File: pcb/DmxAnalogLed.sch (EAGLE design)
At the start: 55 parts, among them IC2 7805TV, J1 RS485, J2 POWER_JACKPTH, J3 RS485, Q1 16MHz 10ppm, U1 ARDUINO_LEONARDO-REV3B_SMARTP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, U2 SN75176ASOIC, X1 USBPTH

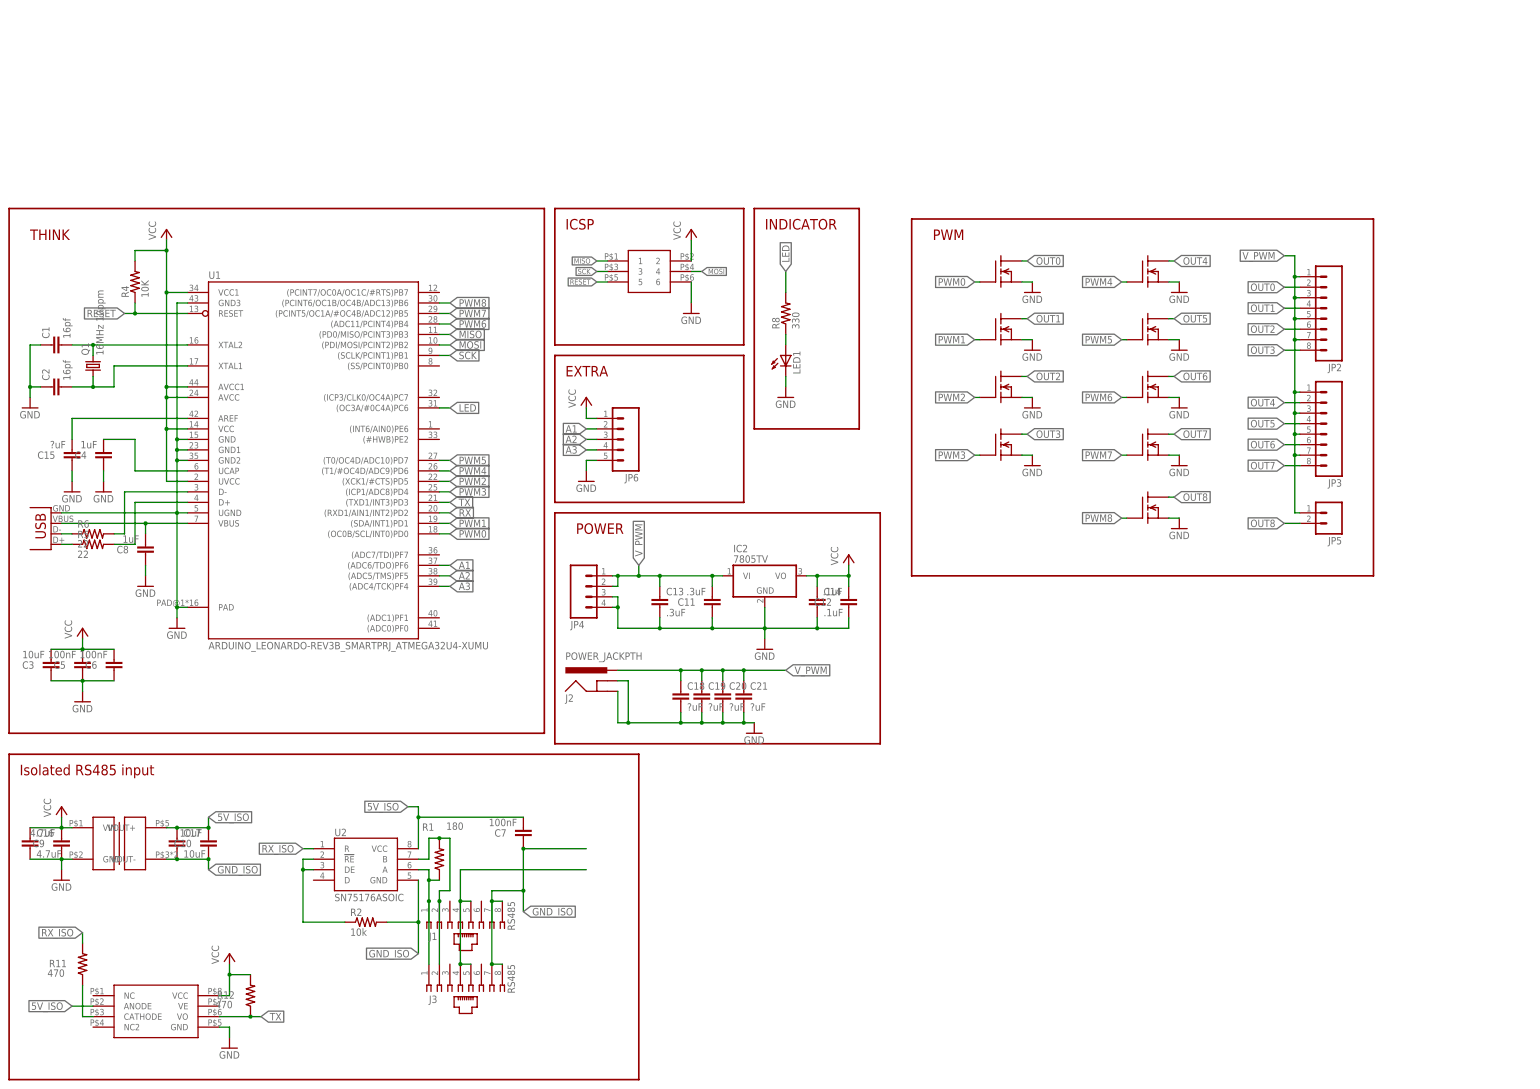
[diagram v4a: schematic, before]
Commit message: Re-wire PWMs for hardware PWM generation. Bugfix: Serial should be connected to AVR RX, not TX
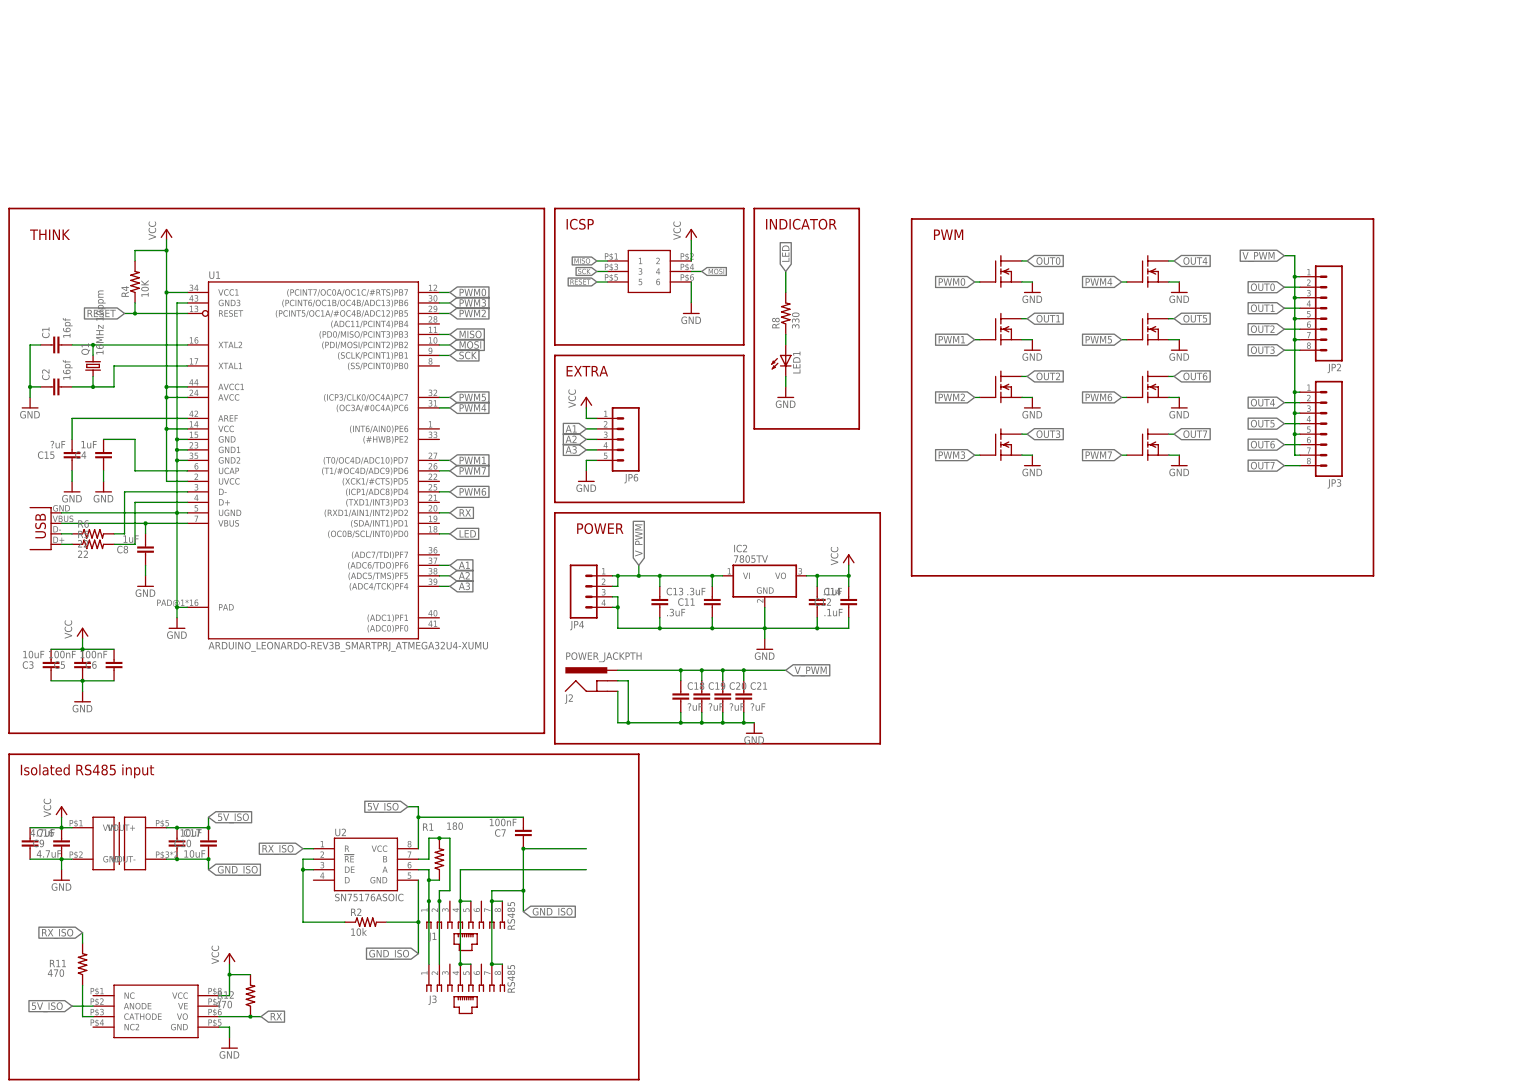
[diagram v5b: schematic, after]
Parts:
- removed JP5: (no value), SparkFun:M023.5MM
- removed U$11: N_MOSFET, blinkiverse:N_MOSFET
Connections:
- removed net OUT8: JP5.2, U$11.D
- removed net PWM8: U$11.G, U1.(PCINT6/OC1B/OC4B/ADC13)PB6
- removed net TX: R12.1, U$12.VO, U1.(TXD1/INT3)PD3
- net GND: no longer U$11.S
- net LED: now also U1.(OC0B/SCL/INT0)PD0; no longer U1.(OC3A/#0C4A)PC6
- net PWM0: now also U1.(PCINT7/OC0A/OC1C/#RTS)PB7; no longer U1.(OC0B/SCL/INT0)PD0
- net PWM1: now also U1.(T0/OC4D/ADC10)PD7; no longer U1.(SDA/INT1)PD1
- net PWM2: now also U1.(PCINT5/OC1A/#OC4B/ADC12)PB5; no longer U1.(XCK1/#CTS)PD5
- net PWM3: now also U1.(PCINT6/OC1B/OC4B/ADC13)PB6; no longer U1.(ICP1/ADC8)PD4
- net PWM4: now also U1.(OC3A/#0C4A)PC6; no longer U1.(T1/#OC4D/ADC9)PD6
- net PWM5: now also U1.(ICP3/CLK0/OC4A)PC7; no longer U1.(T0/OC4D/ADC10)PD7
- net PWM6: now also U1.(ICP1/ADC8)PD4; no longer U1.(ADC11/PCINT4)PB4
- net PWM7: now also U1.(T1/#OC4D/ADC9)PD6; no longer U1.(PCINT5/OC1A/#OC4B/ADC12)PB5
- net RX: now also R12.1, U$12.VO
- net V_PWM: no longer JP5.1
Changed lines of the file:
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@@
 <part name="GND2" library="SparkFun" deviceset="GND" device=""/>
 <part name="P+9" library="supply1" deviceset="VCC" device=""/>
-<part name="U$11" library="blinkiverse" deviceset="N_MOSFET" device=""/>
-<part name="GND8" library="supply1" deviceset="GND" device=""/>
-<part name="JP5" library="SparkFun" deviceset="M02" device="3.5MM"/>
 <part name="C8" library="SparkFun" deviceset="CAP" device="0805" value="1uF"/>
 <part name="GND18" library="supply1" deviceset="GND" device=""/>
@@
 <instance part="GND2" gate="1" x="22.86" y="-124.46"/>
 <instance part="P+9" gate="VCC" x="22.86" y="-101.6"/>
-<instance part="U$11" gate="G$1" x="243.84" y="6.35"/>
-<instance part="GND8" gate="1" x="252.73" y="1.27"/>
-<instance part="JP5" gate="G$1" x="289.56" y="5.08" rot="R180"/>
 <instance part="C8" gate="G$1" x="2.54" y="-2.54" smashed="yes" rot="R180">
 <attribute name="NAME" x="-1.524" y="-2.921" size="1.778" layer="95" rot="R180"/>
@@
 <wire x1="20.32" y1="-119.38" x2="22.86" y2="-119.38" width="0.1524" layer="91"/>
 <wire x1="22.86" y1="-119.38" x2="22.86" y2="-121.92" width="0.1524" layer="91"/>
-</segment>
-<segment>
-<pinref part="U$11" gate="G$1" pin="S"/>
-<wire x1="250.19" y1="3.81" x2="252.73" y2="3.81" width="0.1524" layer="91"/>
-<pinref part="GND8" gate="1" pin="GND"/>
 </segment>
 <segment>
@@
 <label x="76.2" y="5.08" size="1.778" layer="95" xref="yes"/>
 </segment>
-</net>
-<net name="TX" class="0">
-<segment>
-<pinref part="U1" gate="G$1" pin="(TXD1/INT3)PD3"/>
-<wire x1="73.66" y1="7.62" x2="76.2" y2="7.62" width="0.1524" layer="91"/>
-<label x="76.2" y="7.62" size="1.778" layer="95" xref="yes"/>
-</segment>
 <segment>
 <pinref part="U$12" gate="G$1" pin="VO"/>
@@
 </segment>
 <segment>
-<pinref part="U1" gate="G$1" pin="(OC0B/SCL/INT0)PD0"/>
-<wire x1="73.66" y1="0" x2="76.2" y2="0" width="0.1524" layer="91"/>
-<label x="76.2" y="0" size="1.778" layer="95" xref="yes"/>
+<pinref part="U1" gate="G$1" pin="(PCINT7/OC0A/OC1C/#RTS)PB7"/>
+<wire x1="73.66" y1="58.42" x2="76.2" y2="58.42" width="0.1524" layer="91"/>
+<label x="76.2" y="58.42" size="1.778" layer="95" xref="yes"/>
 </segment>
 </net>
@@
 </segment>
 <segment>
-<pinref part="U1" gate="G$1" pin="(SDA/INT1)PD1"/>
-<wire x1="73.66" y1="2.54" x2="76.2" y2="2.54" width="0.1524" layer="91"/>
-<label x="76.2" y="2.54" size="1.778" layer="95" xref="yes"/>
+<pinref part="U1" gate="G$1" pin="(T0/OC4D/ADC10)PD7"/>
+<wire x1="73.66" y1="17.78" x2="76.2" y2="17.78" width="0.1524" layer="91"/>
+<label x="76.2" y="17.78" size="1.778" layer="95" xref="yes"/>
 </segment>
 </net>
@@
 </segment>
 <segment>
-<pinref part="U1" gate="G$1" pin="(XCK1/#CTS)PD5"/>
-<wire x1="73.66" y1="12.7" x2="76.2" y2="12.7" width="0.1524" layer="91"/>
-<label x="76.2" y="12.7" size="1.778" layer="95" xref="yes"/>
+<pinref part="U1" gate="G$1" pin="(PCINT5/OC1A/#OC4B/ADC12)PB5"/>
+<wire x1="73.66" y1="53.34" x2="76.2" y2="53.34" width="0.1524" layer="91"/>
+<label x="76.2" y="53.34" size="1.778" layer="95" xref="yes"/>
 </segment>
 </net>
@@
 </segment>
 <segment>
+<pinref part="U1" gate="G$1" pin="(PCINT6/OC1B/OC4B/ADC13)PB6"/>
+<wire x1="73.66" y1="55.88" x2="76.2" y2="55.88" width="0.1524" layer="91"/>
+<label x="76.2" y="55.88" size="1.778" layer="95" xref="yes"/>
+</segment>
+</net>
+<net name="PWM4" class="0">
+<segment>
+<pinref part="U$6" gate="G$1" pin="G"/>
+<wire x1="240.03" y1="60.96" x2="238.76" y2="60.96" width="0.1524" layer="91"/>
+<label x="238.76" y="60.96" size="1.778" layer="95" rot="R180" xref="yes"/>
+</segment>
+<segment>
+<pinref part="U1" gate="G$1" pin="(OC3A/#0C4A)PC6"/>
+<wire x1="73.66" y1="30.48" x2="76.2" y2="30.48" width="0.1524" layer="91"/>
+<label x="76.2" y="30.48" size="1.778" layer="95" xref="yes"/>
+</segment>
+</net>
+<net name="PWM5" class="0">
+<segment>
+<pinref part="U$7" gate="G$1" pin="G"/>
+<wire x1="240.03" y1="46.99" x2="238.76" y2="46.99" width="0.1524" layer="91"/>
+<label x="238.76" y="46.99" size="1.778" layer="95" rot="R180" xref="yes"/>
+</segment>
+<segment>
+<pinref part="U1" gate="G$1" pin="(ICP3/CLK0/OC4A)PC7"/>
+<wire x1="73.66" y1="33.02" x2="76.2" y2="33.02" width="0.1524" layer="91"/>
+<label x="76.2" y="33.02" size="1.778" layer="95" xref="yes"/>
+</segment>
+</net>
+<net name="PWM6" class="0">
+<segment>
+<pinref part="U$8" gate="G$1" pin="G"/>
+<wire x1="240.03" y1="33.02" x2="238.76" y2="33.02" width="0.1524" layer="91"/>
+<label x="238.76" y="33.02" size="1.778" layer="95" rot="R180" xref="yes"/>
+</segment>
+<segment>
 <pinref part="U1" gate="G$1" pin="(ICP1/ADC8)PD4"/>
 <wire x1="73.66" y1="10.16" x2="76.2" y2="10.16" width="0.1524" layer="91"/>
@@
 </segment>
 </net>
-<net name="PWM4" class="0">
-<segment>
-<pinref part="U$6" gate="G$1" pin="G"/>
-<wire x1="240.03" y1="60.96" x2="238.76" y2="60.96" width="0.1524" layer="91"/>
-<label x="238.76" y="60.96" size="1.778" layer="95" rot="R180" xref="yes"/>
+<net name="PWM7" class="0">
+<segment>
+<pinref part="U$9" gate="G$1" pin="G"/>
+<wire x1="240.03" y1="19.05" x2="238.76" y2="19.05" width="0.1524" layer="91"/>
+<label x="238.76" y="19.05" size="1.778" layer="95" rot="R180" xref="yes"/>
 </segment>
 <segment>
@@
 <wire x1="73.66" y1="15.24" x2="76.2" y2="15.24" width="0.1524" layer="91"/>
 <label x="76.2" y="15.24" size="1.778" layer="95" xref="yes"/>
-</segment>
-</net>
-<net name="PWM5" class="0">
-<segment>
-<pinref part="U$7" gate="G$1" pin="G"/>
-<wire x1="240.03" y1="46.99" x2="238.76" y2="46.99" width="0.1524" layer="91"/>
-<label x="238.76" y="46.99" size="1.778" layer="95" rot="R180" xref="yes"/>
-</segment>
-<segment>
-<pinref part="U1" gate="G$1" pin="(T0/OC4D/ADC10)PD7"/>
-<wire x1="73.66" y1="17.78" x2="76.2" y2="17.78" width="0.1524" layer="91"/>
-<label x="76.2" y="17.78" size="1.778" layer="95" xref="yes"/>
-</segment>
-</net>
-<net name="PWM6" class="0">
-<segment>
-<pinref part="U$8" gate="G$1" pin="G"/>
-<wire x1="240.03" y1="33.02" x2="238.76" y2="33.02" width="0.1524" layer="91"/>
-<label x="238.76" y="33.02" size="1.778" layer="95" rot="R180" xref="yes"/>
-</segment>
-<segment>
-<pinref part="U1" gate="G$1" pin="(ADC11/PCINT4)PB4"/>
-<wire x1="73.66" y1="50.8" x2="76.2" y2="50.8" width="0.1524" layer="91"/>
-<label x="76.2" y="50.8" size="1.778" layer="95" xref="yes"/>
-</segment>
-</net>
-<net name="PWM7" class="0">
-<segment>
-<pinref part="U$9" gate="G$1" pin="G"/>
-<wire x1="240.03" y1="19.05" x2="238.76" y2="19.05" width="0.1524" layer="91"/>
-<label x="238.76" y="19.05" size="1.778" layer="95" rot="R180" xref="yes"/>
-</segment>
-<segment>
-<pinref part="U1" gate="G$1" pin="(PCINT5/OC1A/#OC4B/ADC12)PB5"/>
-<wire x1="73.66" y1="53.34" x2="76.2" y2="53.34" width="0.1524" layer="91"/>
-<label x="76.2" y="53.34" size="1.778" layer="95" xref="yes"/>
 </segment>
 </net>
@@
 <junction x="280.67" y="29.21"/>
 <junction x="280.67" y="24.13"/>
-<wire x1="280.67" y1="19.05" x2="280.67" y2="5.08" width="0.1524" layer="91"/>
-<pinref part="JP5" gate="G$1" pin="1"/>
-<wire x1="280.67" y1="5.08" x2="281.94" y2="5.08" width="0.1524" layer="91"/>
-<junction x="280.67" y="19.05"/>
 </segment>
 <segment>
@@
 </segment>
 </net>
-<net name="PWM8" class="0">
-<segment>
-<pinref part="U$11" gate="G$1" pin="G"/>
-<wire x1="240.03" y1="3.81" x2="238.76" y2="3.81" width="0.1524" layer="91"/>
-<label x="238.76" y="3.81" size="1.778" layer="95" rot="R180" xref="yes"/>
-</segment>
-<segment>
-<pinref part="U1" gate="G$1" pin="(PCINT6/OC1B/OC4B/ADC13)PB6"/>
-<wire x1="73.66" y1="55.88" x2="76.2" y2="55.88" width="0.1524" layer="91"/>
-<label x="76.2" y="55.88" size="1.778" layer="95" xref="yes"/>
-</segment>
-</net>
-<net name="OUT8" class="0">
-<segment>
-<pinref part="U$11" gate="G$1" pin="D"/>
-<wire x1="250.19" y1="8.89" x2="251.46" y2="8.89" width="0.1524" layer="91"/>
-<label x="251.46" y="8.89" size="1.778" layer="95" xref="yes"/>
-</segment>
-<segment>
-<pinref part="JP5" gate="G$1" pin="2"/>
-<wire x1="281.94" y1="2.54" x2="278.13" y2="2.54" width="0.1524" layer="91"/>
-<label x="278.13" y="2.54" size="1.778" layer="95" rot="R180" xref="yes"/>
-</segment>
-</net>
 <net name="N$10" class="0">
 <segment>
@@
 <net name="LED" class="0">
 <segment>
-<pinref part="U1" gate="G$1" pin="(OC3A/#0C4A)PC6"/>
-<wire x1="73.66" y1="30.48" x2="76.2" y2="30.48" width="0.1524" layer="91"/>
-<label x="76.2" y="30.48" size="1.778" layer="95" xref="yes"/>
-</segment>
-<segment>
 <wire x1="157.48" y1="58.42" x2="157.48" y2="63.5" width="0.1524" layer="91"/>
 <label x="157.48" y="63.5" size="1.778" layer="95" rot="R90" xref="yes"/>
 <pinref part="R8" gate="G$1" pin="2"/>
 </segment>
-</net>
+<segment>
+<pinref part="U1" gate="G$1" pin="(OC0B/SCL/INT0)PD0"/>
+<wire x1="76.2" y1="0" x2="73.66" y2="0" width="0.1524" layer="91"/>
+<label x="76.2" y="0" size="1.778" layer="95" xref="yes"/>
+</segment>
+</net>

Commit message: Almost ready for a re-release of RevA
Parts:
- added R10, R13, R14, R15, R16, R3, R7, R9: 10K, SparkFun:RESISTOR
- added R17, R18, R19, R20, R21, R22, R23, R24: 50, SparkFun:RESISTOR
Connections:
- new net PWM0_MID: R10.2, R17.1, U$1.G
- new net PWM1_MID: R19.1, R9.2, U$3.G
- new net PWM2_MID: R20.1, R7.2, U$4.G
- new net PWM3_MID: R21.1, R3.2, U$5.G
- new net PWM4_MID: R13.2, R18.1, U$6.G
- new net PWM5_MID: R14.2, R22.1, U$7.G
- new net PWM6_MID: R15.2, R23.1, U$8.G
- new net PWM7_MID: R16.2, R24.1, U$9.G
- net GND: now also R10.1, R13.1, R14.1, R15.1, R16.1, R3.1, R7.1, R9.1
- net PWM0: now also R17.2; no longer U$1.G
- net PWM1: now also R19.2; no longer U$3.G
- net PWM2: now also R20.2; no longer U$4.G
- net PWM3: now also R21.2; no longer U$5.G
- net PWM4: now also R18.2; no longer U$6.G
- net PWM5: now also R22.2; no longer U$7.G
- net PWM6: now also R23.2; no longer U$8.G
- net PWM7: now also R24.2; no longer U$9.G
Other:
- moved on the sheet: JP2, JP3

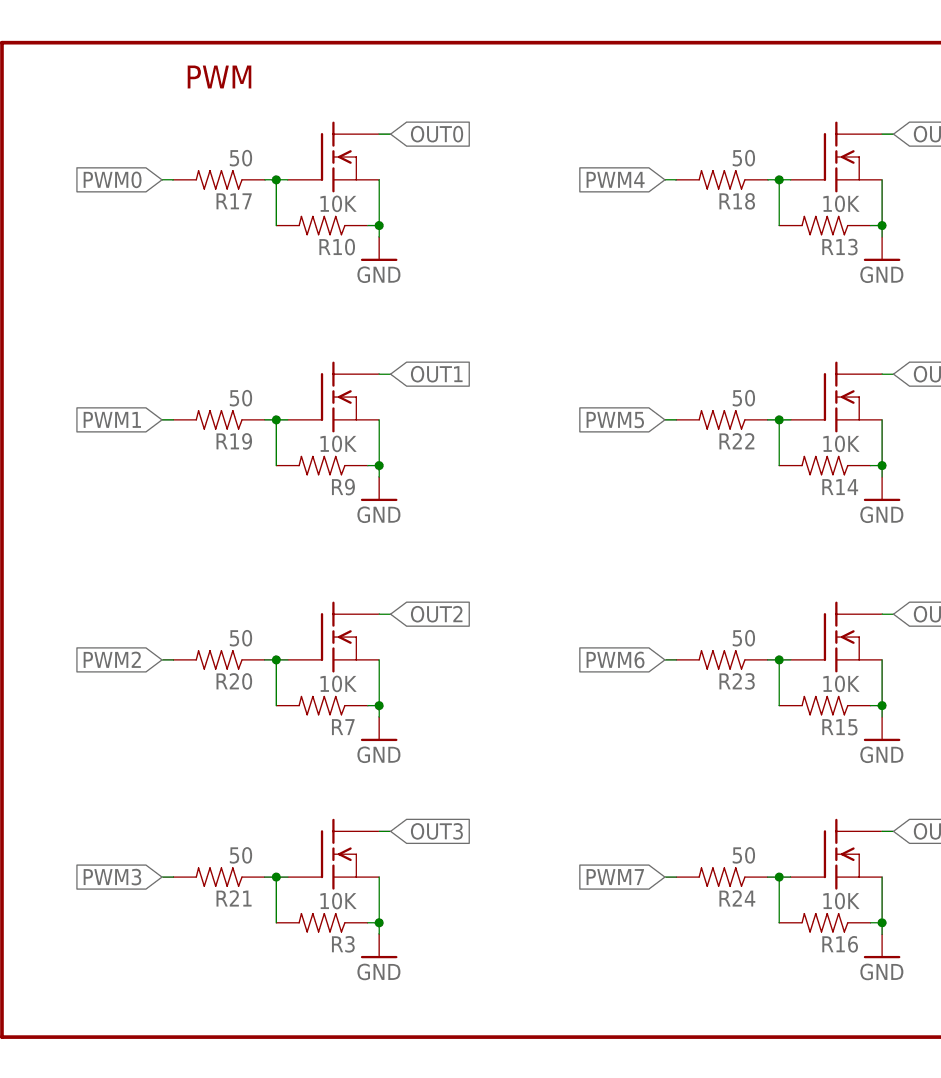
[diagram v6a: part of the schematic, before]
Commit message: Add extra drain vias, space for mounting holes, line up connectors, drop series gate resistors, fix RX line
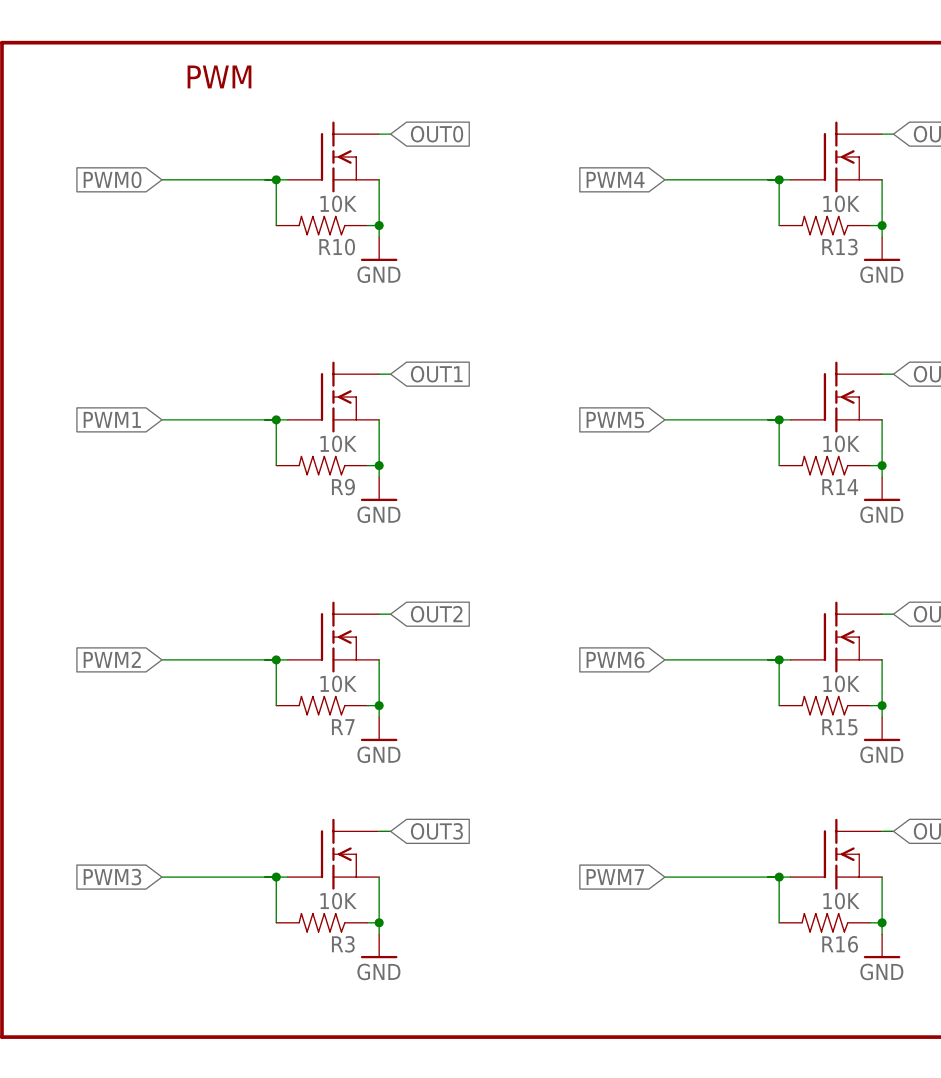
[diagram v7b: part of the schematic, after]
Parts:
- removed R17, R18, R19, R20, R21, R22, R23, R24: 50, SparkFun:RESISTOR
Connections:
- removed net PWM0_MID: R10.2, R17.1, U$1.G
- removed net PWM1_MID: R19.1, R9.2, U$3.G
- removed net PWM2_MID: R20.1, R7.2, U$4.G
- removed net PWM3_MID: R21.1, R3.2, U$5.G
- removed net PWM4_MID: R13.2, R18.1, U$6.G
- removed net PWM5_MID: R14.2, R22.1, U$7.G
- removed net PWM6_MID: R15.2, R23.1, U$8.G
- removed net PWM7_MID: R16.2, R24.1, U$9.G
- net PWM0: now also R10.2, U$1.G; no longer R17.2
- net PWM1: now also R9.2, U$3.G; no longer R19.2
- net PWM2: now also R7.2, U$4.G; no longer R20.2
- net PWM3: now also R3.2, U$5.G; no longer R21.2
- net PWM4: now also R13.2, U$6.G; no longer R18.2
- net PWM5: now also R14.2, U$7.G; no longer R22.2
- net PWM6: now also R15.2, U$8.G; no longer R23.2
- net PWM7: now also R16.2, U$9.G; no longer R24.2
